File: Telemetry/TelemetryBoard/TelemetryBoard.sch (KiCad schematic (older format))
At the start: 44 parts, among them J1 Conn_01x07, J2 Conn_01x02, J3 Micro_SD_Card_Det, J4 Conn_01x04, J5 Conn_01x04, J6 Conn_02x08_Odd_Even, J7 Conn_02x15_Odd_Even, J8 Conn_02x10_Odd_Even, J9 Conn_02x17_Odd_Even, U2 ADM3055E, U3 PQMC3-Dx-Sx-S, U4 CDSOT23-T24CAN

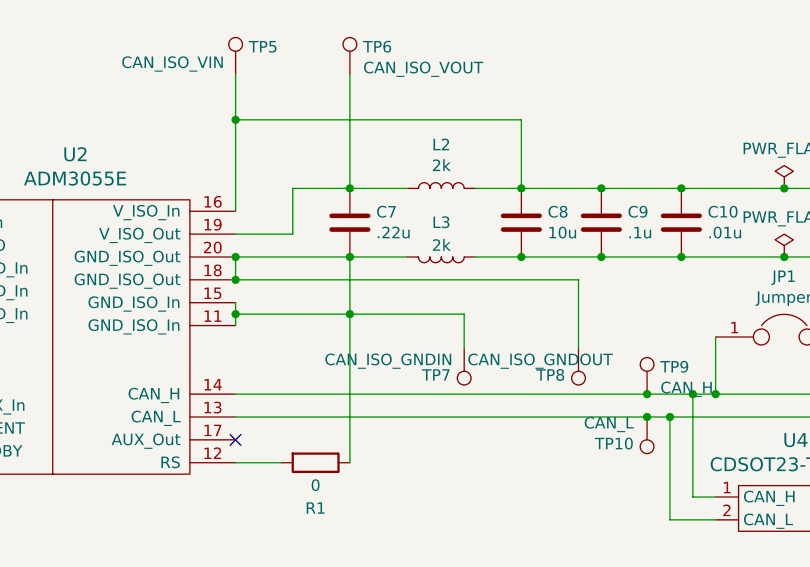
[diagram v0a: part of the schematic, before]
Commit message: Editing Array Board and telemetry board
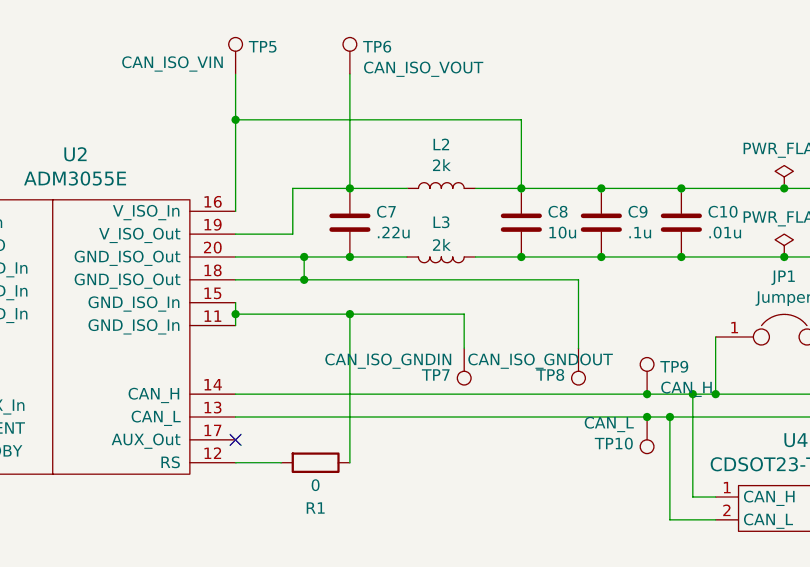
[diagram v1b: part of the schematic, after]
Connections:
- net at C7.2, L3.2, TP8.1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: no longer R1.1, TP7.1, U2.11 (GND_ISO_In), U2.15 (GND_ISO_In)
- new net: R1.1, TP7.1, U2.11 (GND_ISO_In), U2.15 (GND_ISO_In)
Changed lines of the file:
@@
 Connection ~ 8950 1800
 Wire Wire Line
-	7500 2100 7500 2350
-Wire Wire Line
 	7500 3000 7500 2350
-Connection ~ 7000 2200
 Wire Wire Line
 	8500 2200 8500 2500
 Wire Wire Line
-	7000 2200 8500 2200
+	7000 2200 7300 2200
 Wire Wire Line
 	7500 2350 8000 2350
@@
 Wire Wire Line
 	7500 2100 7750 2100
-Connection ~ 7000 2100
-Wire Wire Line
-	7000 2100 7500 2100
+Wire Wire Line
+	7000 2100 7300 2100
 Wire Wire Line
 	7000 2300 7000 2350
-Wire Wire Line
-	7000 2100 7000 2200
 Wire Wire Line
 	7000 3000 7200 3000
@@
 Wire Wire Line
 	3850 5350 3850 5300
+Wire Wire Line
+	7300 2100 7300 2200
+Connection ~ 7300 2100
+Wire Wire Line
+	7300 2100 7500 2100
+Connection ~ 7300 2200
+Wire Wire Line
+	7300 2200 8500 2200
 $EndSCHEMATC

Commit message: Finished Telemetry Board
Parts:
- removed J1: Conn_01x07, Connector_Molex:Molex_Micro-Fit_3.0_43650-0715_1x07_P3.00mm_Vertical, symbol Connector_Generic:Conn_01x07
- removed TP11, TP12: TestPoint, TestPoint:TestPoint_Keystone_5005-5009_Compact, symbol Connector:TestPoint
- added D1: LED, LED_SMD:LED_0805_2012Metric, symbol Device:LED
- added R3: 3k, Resistor_SMD:R_0805_2012Metric, symbol Device:R
- L1: footprint Inductor_SMD:L_0805_2012Metric -> Inductor_SMD:L_TDK_NLV32_3.2x2.5mm; P/N (none) -> DFE322520FD-4R7M-P2
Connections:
- net +9V: now also R3.1
- net GND: now also J8.8 (Pin_8), D1.1 (K)
- net CS: now reaches J3.2 (DAT3/CD)
- net CS: now also J8.16 (Pin_16)
- net MOSI: now reaches J3.3 (CMD)
- net MOSI: now also J8.14 (Pin_14)
- net CLOCK: now reaches J3.5 (CLK)
- net CLOCK: now also J8.10 (Pin_10)
- net MISO: now reaches J3.7 (DAT0)
- net MISO: now also J8.12 (Pin_12)
- net DET: now reaches J3.9 (DET_B)
- net DET: now also J8.20 (Pin_20)
- new net: D1.2 (A), R3.2
- no-connect marks 102 -> 96
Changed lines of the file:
@@
 	1    0    0    -1
-$EndComp
-$Comp
-L Connector_Generic:Conn_01x07 J1
-U 1 1 5E5CE1F3
-P 3150 5950
-F 0 "J1" H 3068 6467 50  0000 C CNN
-F 1 "Conn_01x07" H 3068 6376 50  0000 C CNN
-F 2 "Connector_Molex:Molex_Micro-Fit_3.0_43650-0715_1x07_P3.00mm_Vertical" H 3150 5950 50  0001 C CNN
-F 3 "~" H 3150 5950 50  0001 C CNN
-	1    3150 5950
-	-1   0    0    -1
 $EndComp
 Wire Wire Line
@@
 Wire Wire Line
 	10000 2100 10000 2500
-Connection ~ 9600 1800
 Wire Wire Line
 	10000 2100 10400 2100
 Wire Wire Line
 	10000 1800 10000 2100
-Wire Wire Line
-	9600 1800 10000 1800
 Connection ~ 10100 2200
-Connection ~ 9600 2100
 Wire Wire Line
 	9850 2200 10100 2200
 Wire Wire Line
 	9850 2100 9850 2200
-Wire Wire Line
-	9600 2100 9850 2100
 Wire Wire Line
 	10300 2800 10400 2800
@@
 $EndComp
 $Comp
-L Connector:TestPoint TP12
-U 1 1 5E5CBEE7
-P 9600 2100
-F 0 "TP12" H 9658 2218 50  0000 L CNN
-F 1 "TestPoint" H 9658 2127 50  0000 L CNN
-F 2 "TestPoint:TestPoint_Keystone_5005-5009_Compact" H 9800 2100 50  0001 C CNN
-F 3 "~" H 9800 2100 50  0001 C CNN
-	1    9600 2100
-	1    0    0    -1
-$EndComp
-$Comp
-L Connector:TestPoint TP11
-U 1 1 5E5CB0C5
-P 9600 1800
-F 0 "TP11" H 9658 1918 50  0000 L CNN
-F 1 "TestPoint" H 9658 1827 50  0000 L CNN
-F 2 "TestPoint:TestPoint_Keystone_5005-5009_Compact" H 9800 1800 50  0001 C CNN
-F 3 "~" H 9800 1800 50  0001 C CNN
-	1    9600 1800
-	1    0    0    -1
-$EndComp
-$Comp
 L Connector:TestPoint TP10
 U 1 1 5E5CA08B
@@
 F 0 "L1" V 7340 3850 50  0000 C CNN
 F 1 "5u" V 7249 3850 50  0000 C CNN
-F 2 "Inductor_SMD:L_0805_2012Metric" H 7150 3850 50  0001 C CNN
+F 2 "Inductor_SMD:L_TDK_NLV32_3.2x2.5mm" H 7150 3850 50  0001 C CNN
 F 3 "~" H 7150 3850 50  0001 C CNN
+F 4 "DFE322520FD-4R7M-P2" V 7150 3850 50  0001 C CNN "P/N"
 	1    7150 3850
 	0    -1   -1   0
@@
 L power:GND #PWR013
 U 1 1 5EA61F48
-P 10350 4150
-F 0 "#PWR013" H 10350 3900 50  0001 C CNN
-F 1 "GND" H 10355 3977 50  0000 C CNN
-F 2 "" H 10350 4150 50  0001 C CNN
-F 3 "" H 10350 4150 50  0001 C CNN
-	1    10350 4150
+P 10850 4800
+F 0 "#PWR013" H 10850 4550 50  0001 C CNN
+F 1 "GND" H 10855 4627 50  0000 C CNN
+F 2 "" H 10850 4800 50  0001 C CNN
+F 3 "" H 10850 4800 50  0001 C CNN
+	1    10850 4800
 	1    0    0    -1
 $EndComp
@@
 Wire Wire Line
 	10100 4150 10100 4450
-Connection ~ 10100 4150
-Wire Wire Line
-	10100 4150 10350 4150
 $Comp
 L Connector:TestPoint TP14
@@
 $EndComp
 Connection ~ 9400 1800
-Wire Wire Line
-	9400 1800 9600 1800
 $Comp
 L power:PWR_FLAG #FLG0105
@@
 $EndComp
 Connection ~ 9400 2100
-Wire Wire Line
-	9400 2100 9600 2100
 $Comp
 L Connector_Generic:Conn_02x10_Odd_Even J8
@@
 NoConn ~ 2450 1700
 NoConn ~ 2450 1800
-NoConn ~ 2450 1900
-NoConn ~ 2450 2000
 NoConn ~ 2450 2100
-NoConn ~ 2450 2200
 NoConn ~ 2950 1300
 NoConn ~ 2950 1400
 NoConn ~ 2950 1500
-NoConn ~ 2950 1600
-NoConn ~ 2950 1700
-NoConn ~ 2950 1800
-NoConn ~ 2950 1900
-NoConn ~ 2950 2000
 NoConn ~ 2950 2100
-NoConn ~ 2950 2200
 NoConn ~ 2450 2700
 NoConn ~ 2450 2800
@@
 Wire Wire Line
 	7300 2200 8500 2200
+Text Label 3350 5650 0    50   ~ 0
+CS
+Text Label 3350 5750 0    50   ~ 0
+MOSI
+Text Label 3350 5850 0    50   ~ 0
+VDD
+Text Label 3350 5950 0    50   ~ 0
+CLOCK
+Text Label 3350 6050 0    50   ~ 0
+GND
+Text Label 3350 6150 0    50   ~ 0
+MISO
+NoConn ~ 2450 2200
+NoConn ~ 2450 2000
+NoConn ~ 2450 1900
+Wire Wire Line
+	2950 1700 3050 1700
+Wire Wire Line
+	2950 1800 3050 1800
+Wire Wire Line
+	2950 1900 3050 1900
+Wire Wire Line
+	2950 2000 3050 2000
+Text Label 3050 1600 0    50   ~ 0
+GND
+Text Label 3050 1700 0    50   ~ 0
+CLOCK
+Text Label 3050 1800 0    50   ~ 0
+MISO
+Text Label 3050 1900 0    50   ~ 0
+MOSI
+Text Label 3050 2000 0    50   ~ 0
+CS
+$Comp
+L power:GND #PWR0105
+U 1 1 5E6413A6
+P 3350 1600
+F 0 "#PWR0105" H 3350 1350 50  0001 C CNN
+F 1 "GND" H 3355 1427 50  0000 C CNN
+F 2 "" H 3350 1600 50  0001 C CNN
+F 3 "" H 3350 1600 50  0001 C CNN
+	1    3350 1600
+	1    0    0    -1
+$EndComp
+Wire Wire Line
+	2950 1600 3350 1600
+Text Label 3050 2200 0    50   ~ 0
+DET
+Wire Wire Line
+	2950 2200 3050 2200
+Text Label 3350 6250 0    50   ~ 0
+DET
+Wire Wire Line
+	9400 1800 10000 1800
+Wire Wire Line
+	9400 2100 9850 2100
+$Comp
+L Device:LED D1
+U 1 1 5E678CC6
+P 10850 4450
+F 0 "D1" V 10889 4333 50  0000 R CNN
+F 1 "LED" V 10798 4333 50  0000 R CNN
+F 2 "LED_SMD:LED_0805_2012Metric" H 10850 4450 50  0001 C CNN
+F 3 "~" H 10850 4450 50  0001 C CNN
+	1    10850 4450
+	0    -1   -1   0
+$EndComp
+Wire Wire Line
+	10850 4250 10850 4300
+Connection ~ 10350 3850
+Wire Wire Line
+	10850 4800 10850 4700
+$Comp
+L Device:R R3
+U 1 1 5E6AA86F
+P 10850 4100
+F 0 "R3" H 10920 4146 50  0000 L CNN
+F 1 "3k" H 10920 4055 50  0000 L CNN
+F 2 "Resistor_SMD:R_0805_2012Metric" V 10780 4100 50  0001 C CNN
+F 3 "~" H 10850 4100 50  0001 C CNN
+	1    10850 4100
+	1    0    0    -1
+$EndComp
+Wire Wire Line
+	10850 3850 10850 3950
+Wire Wire Line
+	10350 3850 10850 3850
+Wire Wire Line
+	10100 4150 10550 4150
+Wire Wire Line
+	10550 4150 10550 4700
+Wire Wire Line
+	10550 4700 10850 4700
+Connection ~ 10100 4150
+Connection ~ 10850 4700
+Wire Wire Line
+	10850 4700 10850 4600
 $EndSCHEMATC
